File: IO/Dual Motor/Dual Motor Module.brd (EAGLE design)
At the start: 32.4 x 24.8 mm, 17 parts, among them U1 PCA9685, U2 DRV8837, U3 DRV8837, U7 TPS62142

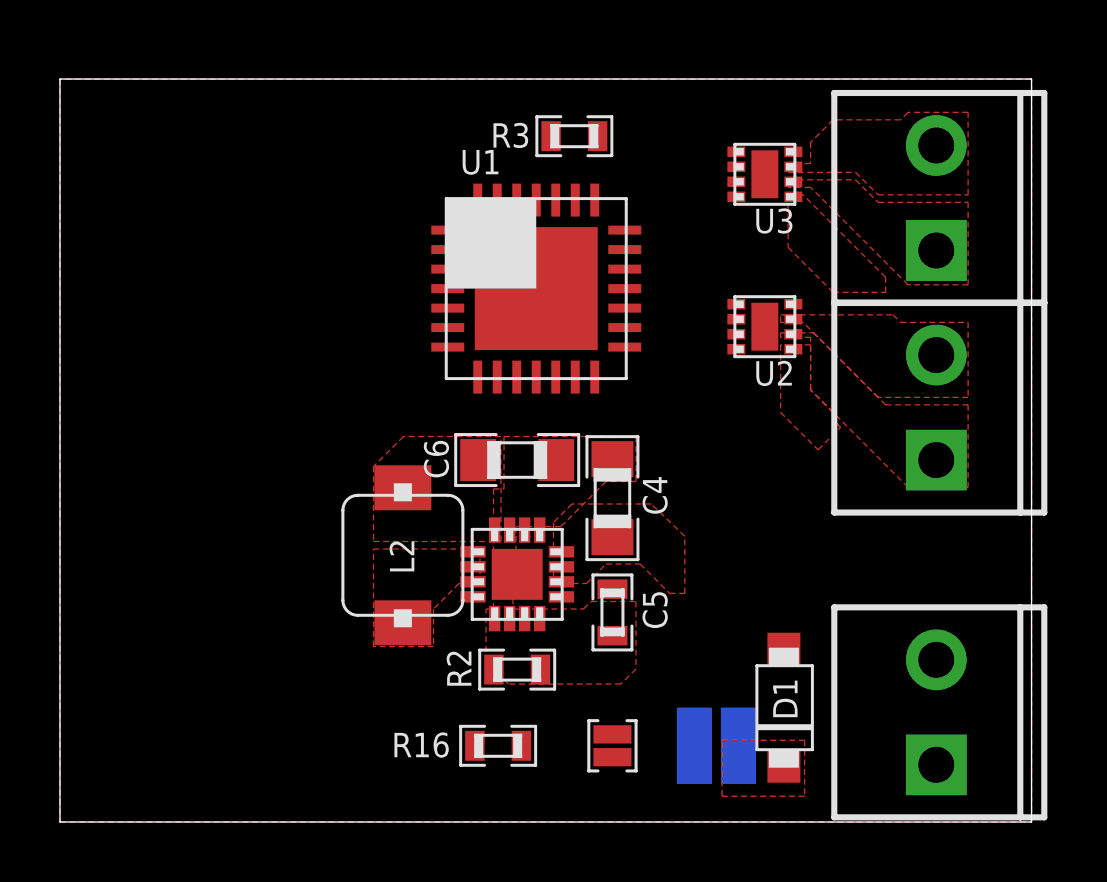
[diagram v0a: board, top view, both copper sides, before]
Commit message: Created Dual Motor Module. Schematic complete, components laid out, routing still needed.
Signed-off-by: Cruz Monrreal II <Cruz.Monrreal@gmail.com>
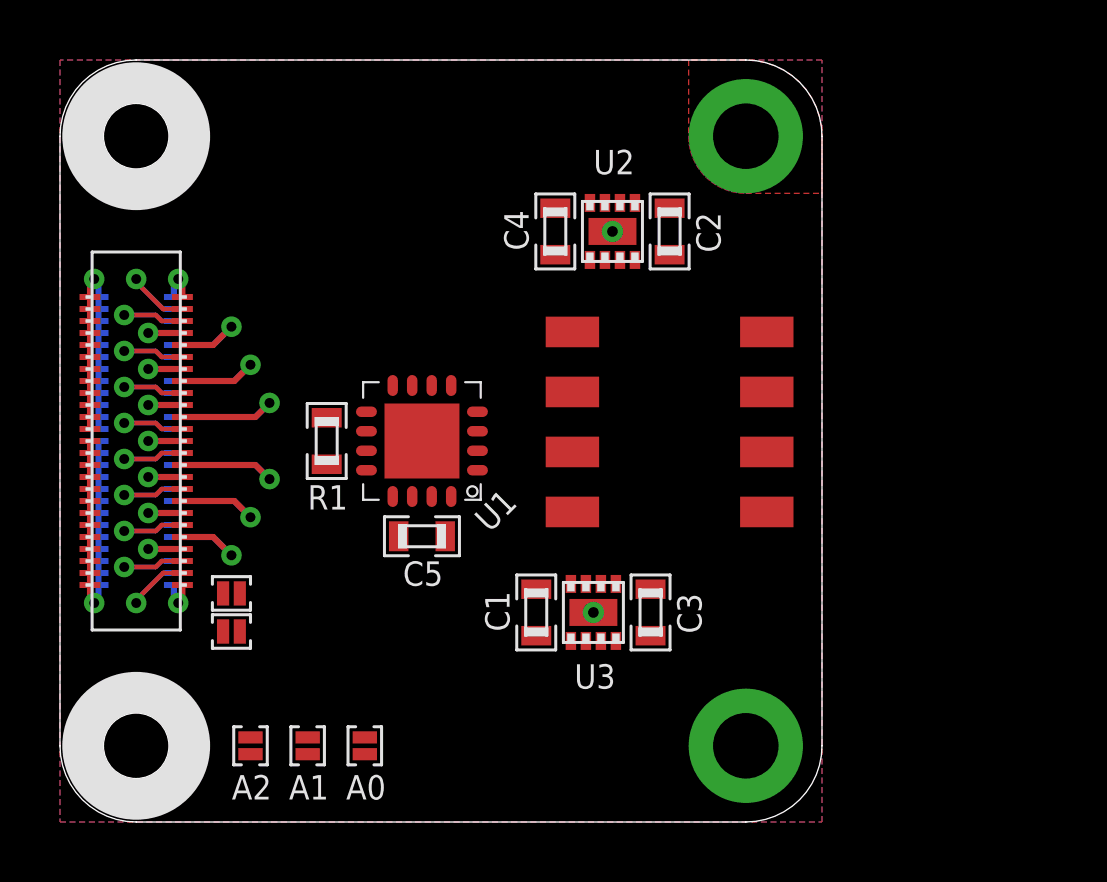
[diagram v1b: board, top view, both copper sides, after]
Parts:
- removed C6: 10uF, .standardparts:0805
- removed D1: (no value), nxp:SOD123W
- removed J1: (no value), .solderjumper:2.XL
- removed J2: (no value), .solderjumper:2.LRG.PASTE
- removed JP1, JP2, JP3: (no value), SparkFun:SCREWTERMINAL-3.5MM-2
- removed L2: 2.2uH, bourns:SRP4020
- removed R16, R2: 100k, .standardparts:0603
- removed R3: 10k, .standardparts:0603
- removed U7: TPS62142, .packages(ti):RGT
- added A0, A1, A2, J4, J5: (no value), .solderjumper:2.MED
- added C1, C2: .1uF, .standardparts:0603
- added C3: 1uF, .standardparts:0603
- added R1: 47k, .standardparts:0603
- added U$2: ROOT1.BOTH, thinkmaketest:ROOT1.BOTH
- added U$3, U$4: HOLE.#2, .screw_holes:#2
- added U$9: HEADER.1X4.MMS-104-02-X-SH, samtec:MMS-104-02-X-SH
- C4: value 10uF -> 1uF; device .standardparts:0805 -> .standardparts:0603
- C5: value 3.3nF -> .1uF
- U1: value PCA9685 -> MSP430G2452.QFN16; device nxp:HVQFN28 -> TI_MSP430_v16:RSA16
- moved U3 15.7 mm to (17.8, 6.99), turned to 270 degrees
- moved C4 9.09 mm to (16.5, 19.7)
- moved C5 6.84 mm to (12.1, 9.53), turned to 180 degrees
- moved U1 6.35 mm to (12.1, 12.7), turned to 180 degrees
- moved U2 5.99 mm to (18.4, 19.7), turned to 90 degrees
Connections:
- removed net 3.3V.EN: J2.1, R16.1, U7.13
- removed net B: U1.17
- removed net EN: R3.1, U1.23
- removed net G: U1.18
- removed net M0.1: U1.6, U2.6
- removed net M0.2: U1.7, U2.5
- removed net M1.1: U1.8, U3.6
- removed net M1.2: U1.9, U3.5
- removed net M2.1: U1.10
- removed net M2.2: U1.11
- removed net M3.1: U1.12
- removed net M3.2: U1.13
- removed net MOTOR.EN: U1.15, U2.7, U3.7
- removed net R: U1.16
- removed net SVRO0: U1.19
- removed net SVRO1: U1.20
- removed net SVRO2: U1.21
- removed net SVRO3: U1.22
- removed net VBAT: D1.P$2, J1.1
- new net !RST: J4.1, R1.2, U1.9
- new net !SLP: U1.1, U2.7, U3.7
- new net M0+: U$9.1, U$9.1@1, U2.2
- new net M0-: U$9.2, U$9.2@1, U2.3
- new net M0.A: U1.2, U2.6
- new net M0.B: U1.3, U2.5
- new net M1+: U$9.3, U$9.3@1, U3.2
- new net M1-: U$9.4, U$9.4@1, U3.3
- new net M1.A: U1.4, U3.6
- new net M1.B: U1.5, U3.5
- new net N$10: U$2.01, U$2.01@1, U$2.01@VIA
- new net N$11: U$2.02, U$2.02@1, U$2.02@VIA
- new net N$13: U$2.ADC0, U$2.ADC0@1, U$2.ADC0@VIA
- new net N$16: U$2.07, U$2.07@1, U$2.07@VIA
- new net N$17: U$2.WAKE, U$2.WAKE@1, U$2.WAKE@VIA
- new net N$18: U$2.TDI, U$2.TDI@1, U$2.TDI@VIA
- new net N$19: U$2.TDO, U$2.TDO@1, U$2.TDO@VIA
- new net N$20: J5.2, U$2.TCK, U$2.TCK@1, U$2.TCK@VIA
- new net N$21: U$2.TMS, U$2.TMS@1, U$2.TMS@VIA
- new net N$22: U$2.TRST, U$2.TRST@1, U$2.TRST@VIA
- new net N$23: U$2.RXI.DBG, U$2.RXI.DBG@1, U$2.RXI.DBG@VIA
- new net N$24: U$2.TXO.DBG, U$2.TXO.DBG@1, U$2.TXO.DBG@VIA
- new net N$25: J4.2, U$2.RST, U$2.RST@1, U$2.RST@VIA
- new net N$26: A2.1, U1.12
- new net N$3: A0.2, U1.6
- new net N$5: U$2.03, U$2.03@1, U$2.03@VIA
- new net N$8: U$2.TXO, U$2.TXO@1, U$2.TXO@VIA
- new net N$9: U$2.RXI, U$2.RXI@1, U$2.RXI@VIA
- new net TEST: J5.1, U1.10
- net 3.3V: now also C1.1, C2.1, C5.1, R1.1, U$2.3.3V@1, U$2.3.3V@10, U$2.3.3V@11, U$2.3.3V@12, U$2.3.3V@13, U$2.3.3V@14, U$2.3.3V@15, U$2.3.3V@16, U$2.3.3V@17, U$2.3.3V@18, U$2.3.3V@19, U$2.3.3V@2, U$2.3.3V@20, U$2.3.3V@21, U$2.3.3V@22, U$2.3.3V@23, U$2.3.3V@24, U$2.3.3V@3, U$2.3.3V@4, U$2.3.3V@5, U$2.3.3V@6, U$2.3.3V@7, U$2.3.3V@8, U$2.3.3V@9, U$2.3.3V@VIA, U1.15, U1.16; no longer C6.1, L2.2, R2.1, R3.2, U1.24, U1.28, U1.4, U1.5, U7.14
- net GND: now also A0.1, A1.2, A2.2, C1.2, C2.2, C3.2, U$2.GND@1, U$2.GND@10, U$2.GND@11, U$2.GND@12, U$2.GND@13, U$2.GND@14, U$2.GND@15, U$2.GND@16, U$2.GND@17, U$2.GND@18, U$2.GND@19, U$2.GND@2, U$2.GND@20, U$2.GND@21, U$2.GND@22, U$2.GND@23, U$2.GND@24, U$2.GND@25, U$2.GND@26, U$2.GND@3, U$2.GND@4, U$2.GND@5, U$2.GND@6, U$2.GND@7, U$2.GND@8, U$2.GND@9, U$2.GND@VIA, U1.13, U1.TP; no longer C6.2, JP1.1, R16.2, U1.1, U1.2, U1.25, U1.3, U1.PAD, U7.15, U7.16, U7.5, U7.6, U7.7, U7.8, U7.PAD
- net N$1: now also U$2.04, U$2.04@1, U$2.04@VIA; no longer JP2.1, U2.2
- net N$12: now also U$2.MOSI, U$2.MOSI@1, U$2.MOSI@VIA; no longer L2.1, U7.1, U7.2, U7.3
- net N$14: now also U$2.05, U$2.05@1, U$2.05@VIA; no longer R2.2, U7.4
- net N$15: now also U$2.06, U$2.06@1, U$2.06@VIA; no longer C5.1, U7.9
- net N$2: now also U$2.ADC1, U$2.ADC1@1, U$2.ADC1@VIA; no longer D1.P$1, JP1.2
- net N$4: now also A1.1, U1.11; no longer JP2.2, U2.3
- net N$6: now also U$2.MISO, U$2.MISO@1, U$2.MISO@VIA; no longer JP3.1, U3.2
- net N$7: now also U$2.SCLK, U$2.SCLK@1, U$2.SCLK@VIA; no longer JP3.2, U3.3
- net SCL: now also U$2.SCL, U$2.SCL@1, U$2.SCL@VIA, U1.8; no longer U1.26
- net SDA: now also U$2.SDA, U$2.SDA@1, U$2.SDA@VIA, U1.7; no longer U1.27
- net VIN: now also C3.1; no longer J1.2, J2.2, U7.10, U7.11, U7.12
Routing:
- removed copper zone on layer 1, net 3.3V
- removed copper zone on layer 1, net N$1
- removed copper zone on layer 1, net N$12
- removed copper zone on layer 1, net N$4
- removed copper zone on layer 1, net N$6
- removed copper zone on layer 1, net N$7
- removed copper zone on layer 1, net VBAT
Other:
- board size 32.4 x 24.8 mm -> 25.4 x 25.4 mm
- board text added: "AnomalousMaker.com"
- board text added: "Cruz Monrreal II"
- board text added: "v1"
- board text removed: "+"
- board text removed: "-"
- board text removed: "3.3v"
- board text removed: "M0"
- board text removed: "M1"

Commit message: Updated silkscreen on Dual Motor Module
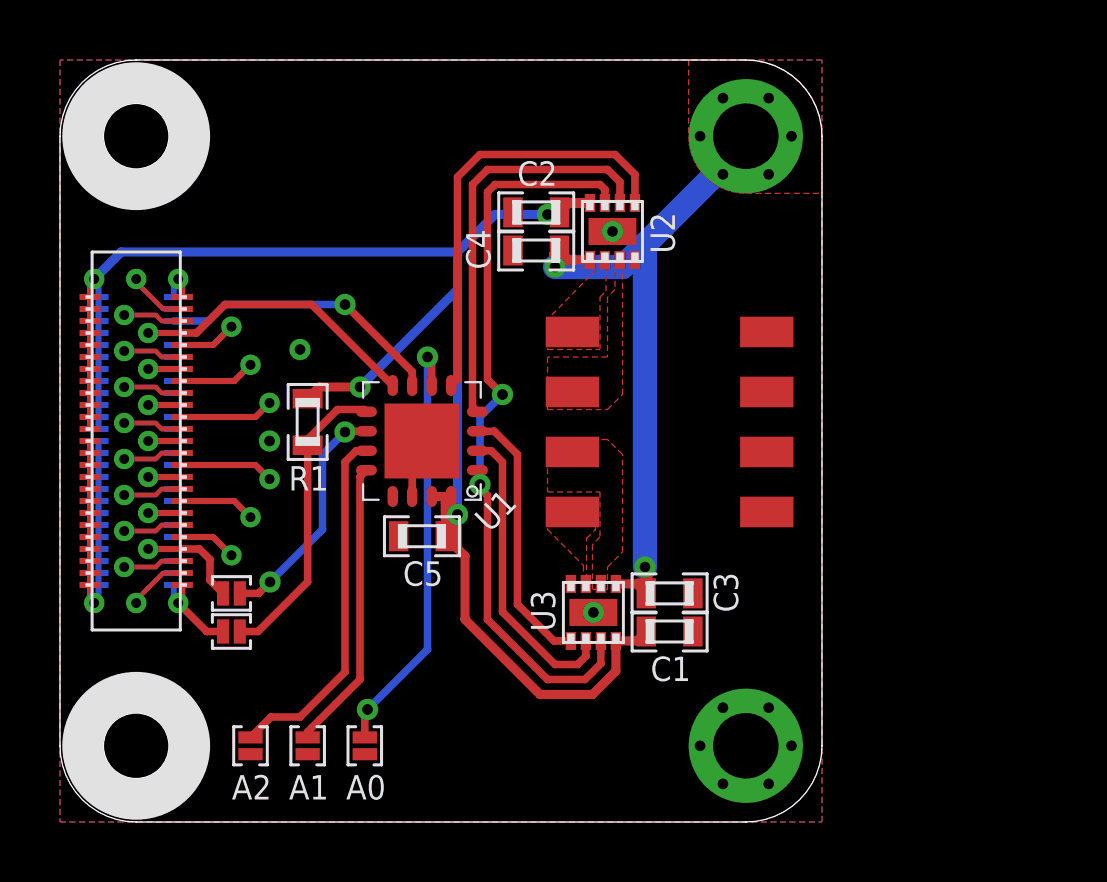
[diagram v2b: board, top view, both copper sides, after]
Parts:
- moved C1 4.49 mm to (20.3, 6.35), turned to 0 degrees
- moved C2 4.49 mm to (15.9, 20.3), turned to 180 degrees
- moved C3 0.90 mm to (20.3, 7.62), turned to 0 degrees
- moved R1 0.90 mm to (8.26, 13.3), turned to 270 degrees
- moved C4 0.90 mm to (15.9, 19.1), turned to 180 degrees
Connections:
- net M0.A: now also U1.4; no longer U1.2
- net M0.B: now also U1.5; no longer U1.3
- net M1.A: now also U1.2; no longer U1.4
- net M1.B: now also U1.3; no longer U1.5
- net N$26: now also A1.1; no longer A2.1
- net N$4: now also A2.1; no longer A1.1
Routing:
- net 3.3V: track 0.00 -> 48.9 mm, vias 0 -> 3
- net !SLP: track 0.00 -> 25.5 mm, vias 0 -> 2
- net VIN: track 0.00 -> 22.9 mm, vias 1 -> 9
- net N$3: track 0.00 -> 14.6 mm, vias 0 -> 2
- net M0.B: track 0.00 -> 14.5 mm
- net M0.A: track 0.00 -> 13.6 mm
- net N$4: track 0.00 -> 11.9 mm
- net M1.A: track 0.00 -> 10.1 mm
- net !RST: track 0.00 -> 10.1 mm
- net N$26: track 0.00 -> 9.72 mm
- net SDA: track 0.00 -> 9.56 mm, vias 0 -> 1
- net M1.B: track 0.00 -> 8.94 mm
- net SCL: track 0.00 -> 8.52 mm
- net TEST: track 0.00 -> 7.92 mm, vias 0 -> 2
- net N$20: track 0.00 -> 2.38 mm
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- added copper zone on layer 1, net M0+
- added copper zone on layer 1, net M0-
- added copper zone on layer 1, net M1+
- added copper zone on layer 1, net M1-
